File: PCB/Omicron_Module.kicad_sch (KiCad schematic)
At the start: 51 parts, among them J1 In, J2 Out, Q1 MJD44H11, Q2 MJD45H11, Q3 MJD44H11, Q4 MJD45H11, U1 NE5532

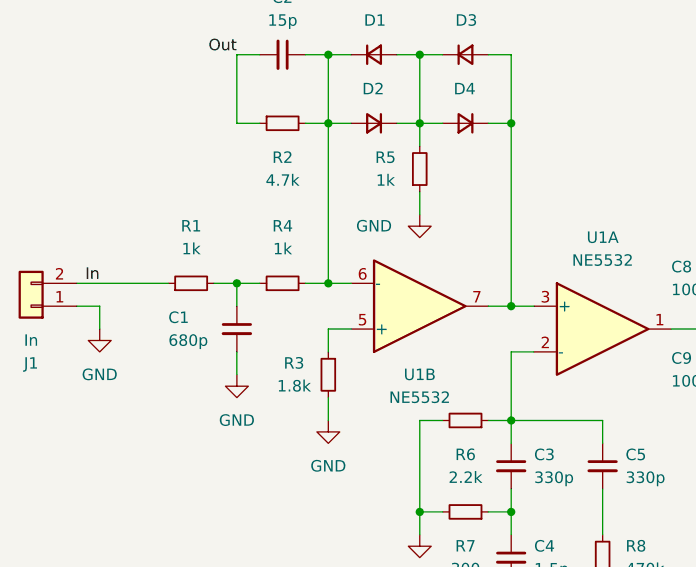
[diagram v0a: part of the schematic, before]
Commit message: Updated resistor values
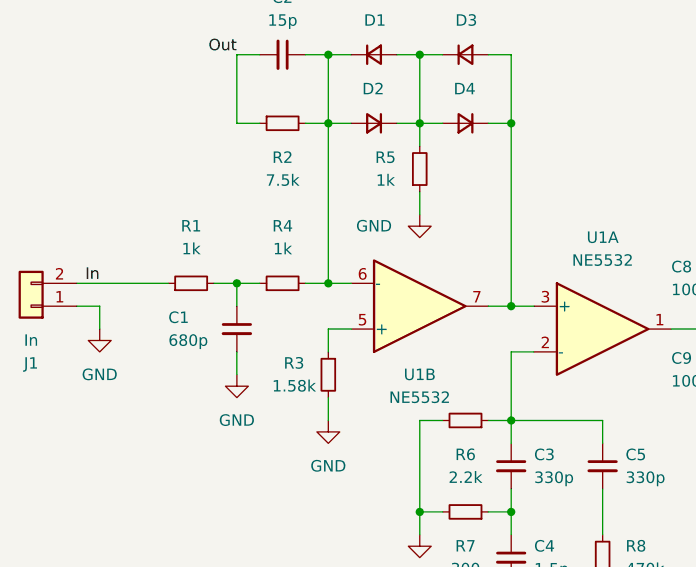
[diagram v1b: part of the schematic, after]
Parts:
- R2: value 4.7k -> 7.5k
- R3: value 1.8k -> 1.58k
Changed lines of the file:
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@@
     (in_bom yes) (on_board yes) (fields_autoplaced)
     (property "Reference" "R3" (id 0) (at 52.07 74.9299 0))
-    (property "Value" "1.8k" (id 1) (at 52.07 77.4699 0))
+    (property "Value" "1.58k" (id 1) (at 52.07 77.4699 0))
     (property "Footprint" "Resistor_SMD:R_1206_3216Metric" (id 2) (at 55.88 76.2 0)
       (effects (font (size 1.27 1.27)) hide)
@@
     (in_bom yes) (on_board yes) (fields_autoplaced)
     (property "Reference" "R2" (id 0) (at 50.8 52.07 90))
-    (property "Value" "4.7k" (id 1) (at 50.8 54.61 90))
+    (property "Value" "7.5k" (id 1) (at 50.8 54.61 90))
     (property "Footprint" "Resistor_SMD:R_1206_3216Metric" (id 2) (at 50.8 48.26 0)
       (effects (font (size 1.27 1.27)) hide)
@@
     )
     (path "/7fbdd09b-d86c-4abb-a312-f9e5bb2e31ec"
-      (reference "R2") (unit 1) (value "4.7k") (footprint "Resistor_SMD:R_1206_3216Metric")
+      (reference "R2") (unit 1) (value "7.5k") (footprint "Resistor_SMD:R_1206_3216Metric")
     )
     (path "/29b7865a-1d33-42a4-a4e9-8eed77c527f3"
-      (reference "R3") (unit 1) (value "1.8k") (footprint "Resistor_SMD:R_1206_3216Metric")
+      (reference "R3") (unit 1) (value "1.58k") (footprint "Resistor_SMD:R_1206_3216Metric")
     )
     (path "/4ae6ce55-670a-4c1c-92ab-18b7f565ee1d"
